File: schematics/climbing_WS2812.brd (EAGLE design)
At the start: 31.8 x 15.2 mm, 8 parts

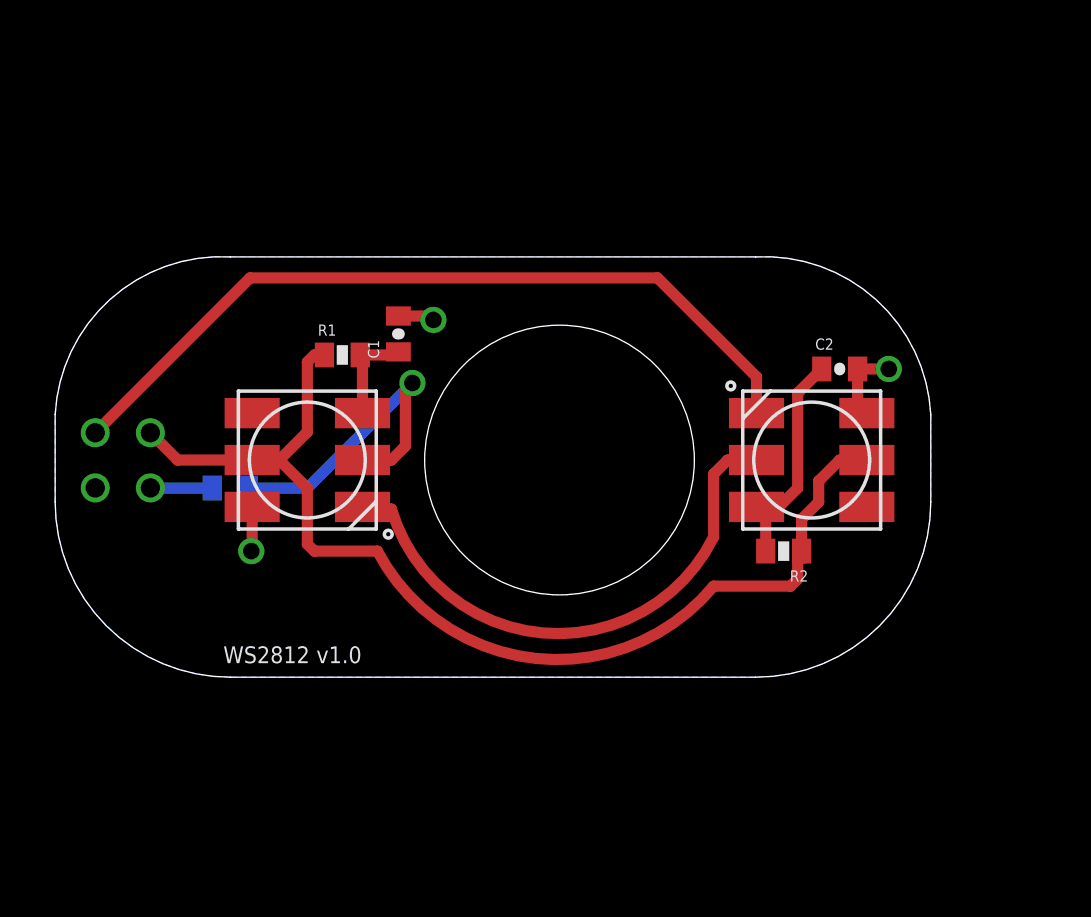
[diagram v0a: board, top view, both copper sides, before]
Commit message: added anti-spinning technology
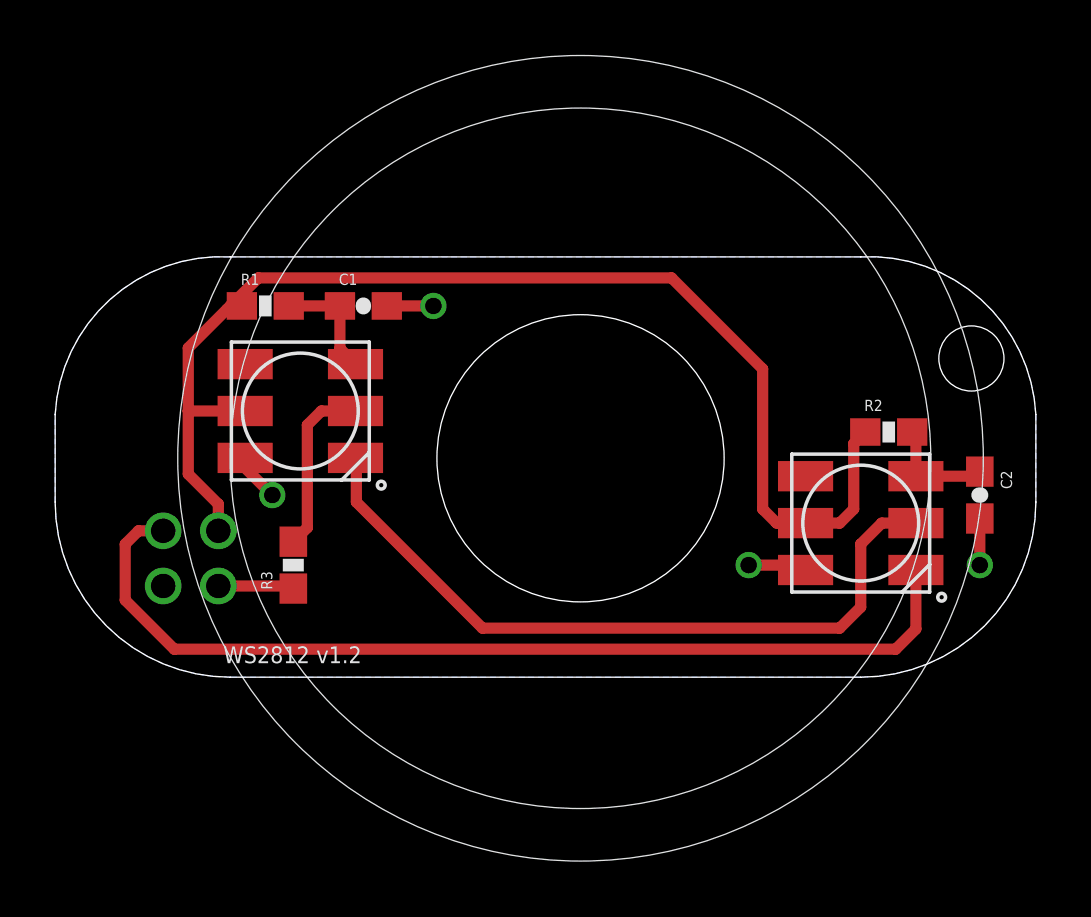
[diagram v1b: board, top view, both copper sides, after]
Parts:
- C1, C2: device SparkFun-Passives:0402-CAP -> SparkFun-Capacitors:0603-CAP
- R1, R2, R3: device SparkFun-Passives:0402-RES -> SparkFun-Passives:0603-RES
- moved C2 6.83 mm to (33.5, 6.60), turned to 270 degrees
- moved R2 5.76 mm to (30.2, 8.89), turned to 0 degrees
- moved U$1 4.33 mm to (4.88, 4.32)
- moved R3 3.61 mm to (8.64, 4.06), flipped to the top, turned to 90 degrees
- moved R1 3.31 mm to (7.62, 13.5)
- moved U$3 2.90 mm to (29.2, 5.59), turned to 0 degrees
- moved U$2 1.80 mm to (8.89, 9.65)
- moved C1 1.63 mm to (11.2, 13.5), turned to 0 degrees
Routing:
- net DODI: track 16.9 -> 26.7 mm
- net VDD: track 37.8 -> 44.6 mm
- net N$2: track 29.1 -> 35.5 mm
- net DI: track 11.7 -> 6.56 mm, vias 1 -> 0
- net VCC2: track 8.20 -> 4.04 mm
- net GND: track 5.81 -> 7.27 mm, vias 3 -> 4
- net VCC: track 3.57 -> 4.20 mm
- net N$1: track 2.25 -> 2.76 mm
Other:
- board size 31.8 x 15.2 mm -> 35.6 x 15.2 mm
- board text added: "WS2812 v1.2"
- board text removed: "WS2812 v1.0"

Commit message: changed WS2812 controller to uUSB, minor spacing edits to everything else
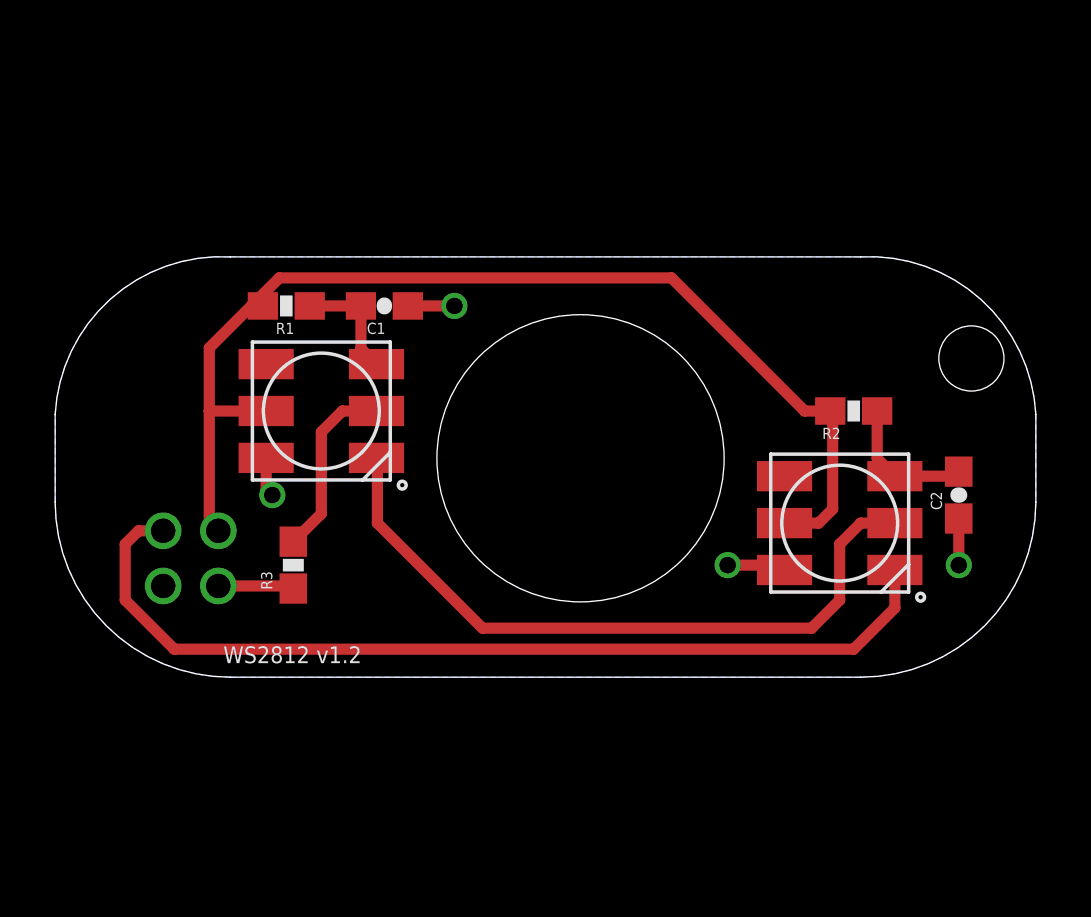
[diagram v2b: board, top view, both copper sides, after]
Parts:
- moved R2 1.48 mm to (29.0, 9.65)
- moved C1 0.76 mm to (11.9, 13.5)
- moved C2 0.76 mm to (32.8, 6.60)
- moved U$3 0.76 mm to (28.4, 5.59)
- moved R1 0.76 mm to (8.38, 13.5)
- moved U$2 0.76 mm to (9.65, 9.65)
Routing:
- net VDD: track 44.6 -> 40.3 mm
- net DODI: track 26.7 -> 25.5 mm
- net N$2: track 35.5 -> 34.3 mm
- net VCC2: track 4.04 -> 5.02 mm
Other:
- board text added: "-"
- board text added: "in"
